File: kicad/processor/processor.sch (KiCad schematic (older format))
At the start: 24 parts

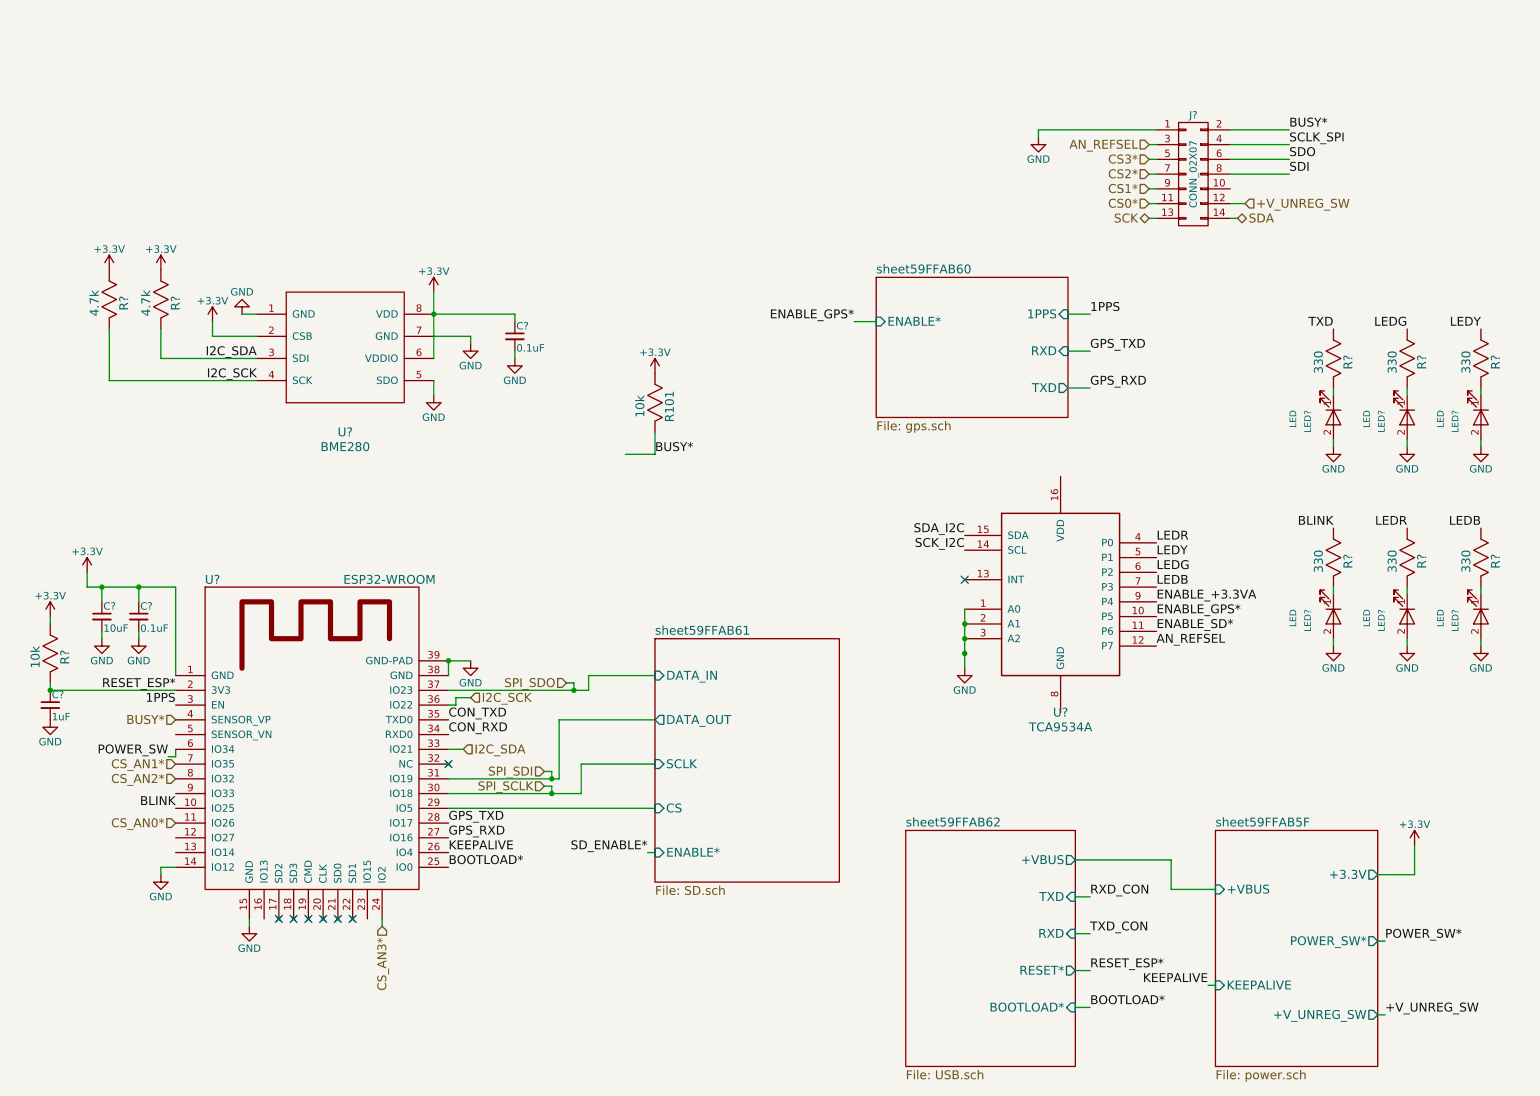
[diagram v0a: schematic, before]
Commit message: Finish split projects, fix ERC, import outline to processor board
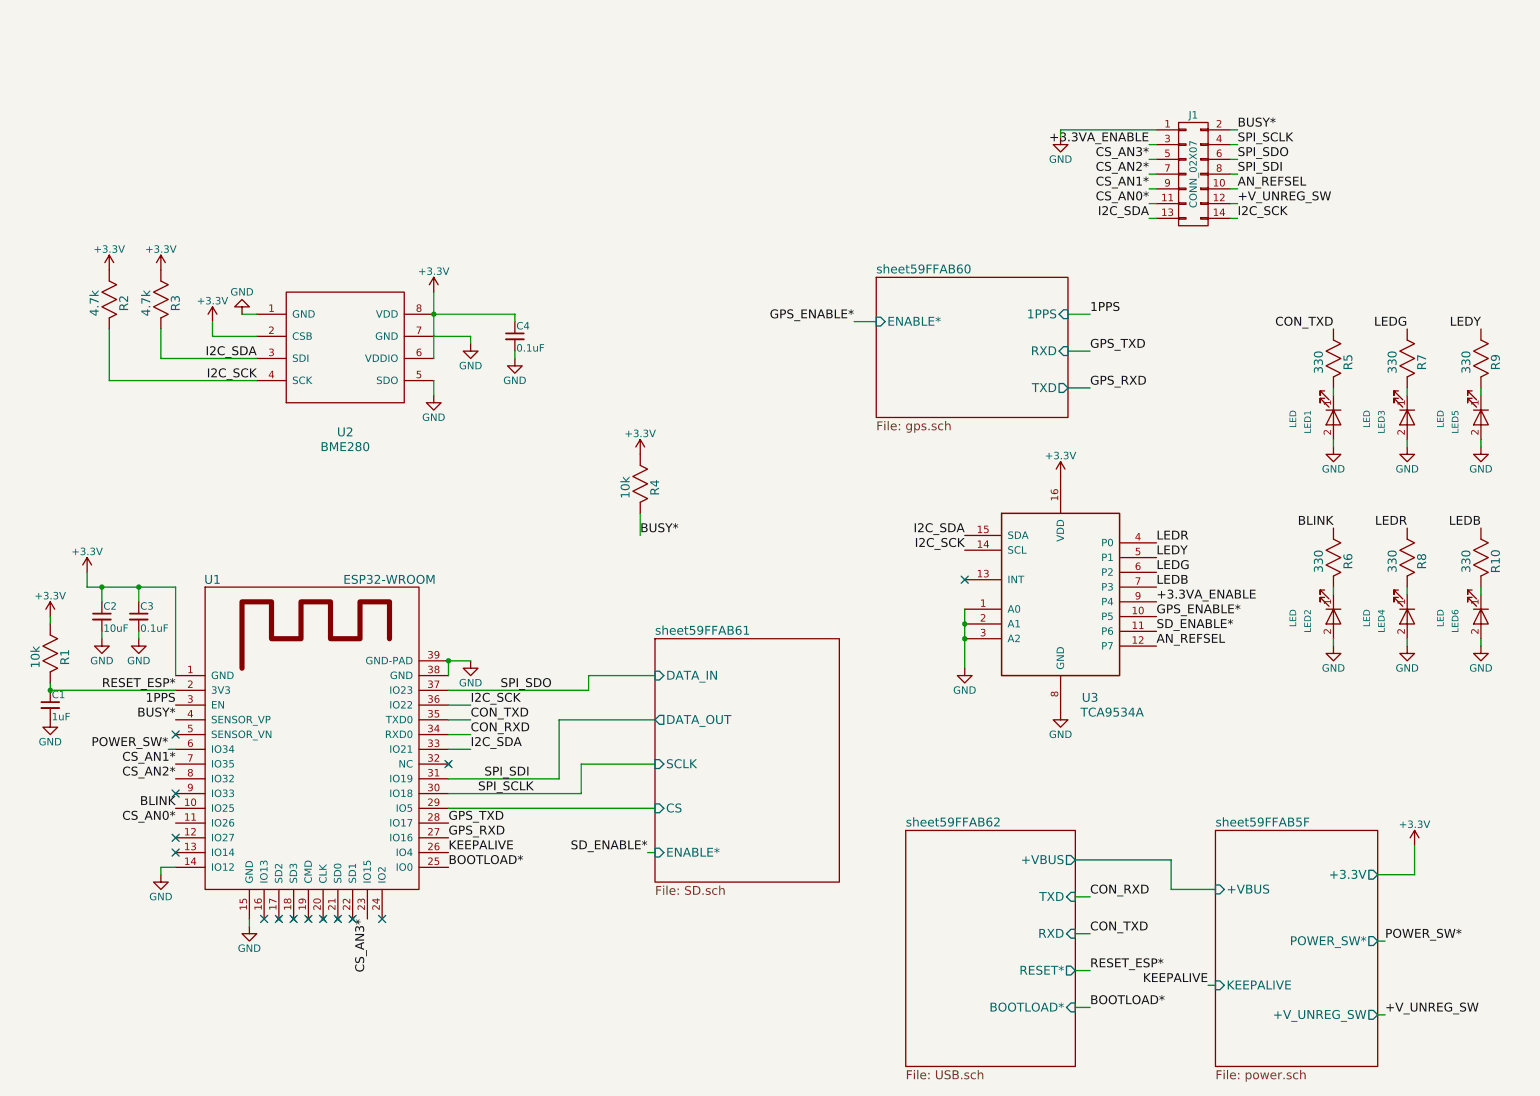
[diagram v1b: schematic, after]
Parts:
- gave numbers to parts that had none: 23
- renumbered R101 to R4
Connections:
- net CS0* is gone; now on net CS_AN0*: J1.11 (P11)
- net CS1* is gone; now on net CS_AN1*: J1.9 (P9)
- net CS2* is gone; now on net CS_AN2*: J1.7 (P7)
- net CS3* is gone; now on net CS_AN3*: J1.5 (P5)
- net ENABLE_SD* is gone; now on net SD_ENABLE*: U3.11 (P6)
- net POWER_SW is gone; now on net POWER_SW*: U1.6 (IO34)
- net SCK is gone; now on net I2C_SDA: J1.13 (P13)
- net SCK_I2C is gone; now on net I2C_SCK: U3.14 (SCL)
- net SCLK_SPI is gone; now on net SPI_SCLK: J1.4 (P4)
- net SDA is gone; now on net I2C_SCK: J1.14 (P14)
- net SDA_I2C is gone; now on net I2C_SDA: U3.15 (SDA)
- net SDI is gone; now on net SPI_SDI: J1.8 (P8)
- net SDO is gone; now on net SPI_SDO: J1.6 (P6)
- net TXD is gone; now on net CON_TXD: R5.1
- net +3V3: now also U3.16 (VDD)
- net AN_REFSEL: now also J1.10 (P10); no longer J1.3 (P3)
- net CS_AN3*: now also U1.23 (IO15); no longer U1.24 (IO2)
- net GND: now also U3.8 (GND)
- net ENABLE_+3.3VA renamed +3.3VA_ENABLE
- net +3.3VA_ENABLE: now also J1.3 (P3)
- net ENABLE_GPS* renamed GPS_ENABLE*
- no-connect marks 8 -> 14
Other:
- moved on the sheet: R4

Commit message: Logic board standalone about done, changed to 0603 resistors and 0805 caps
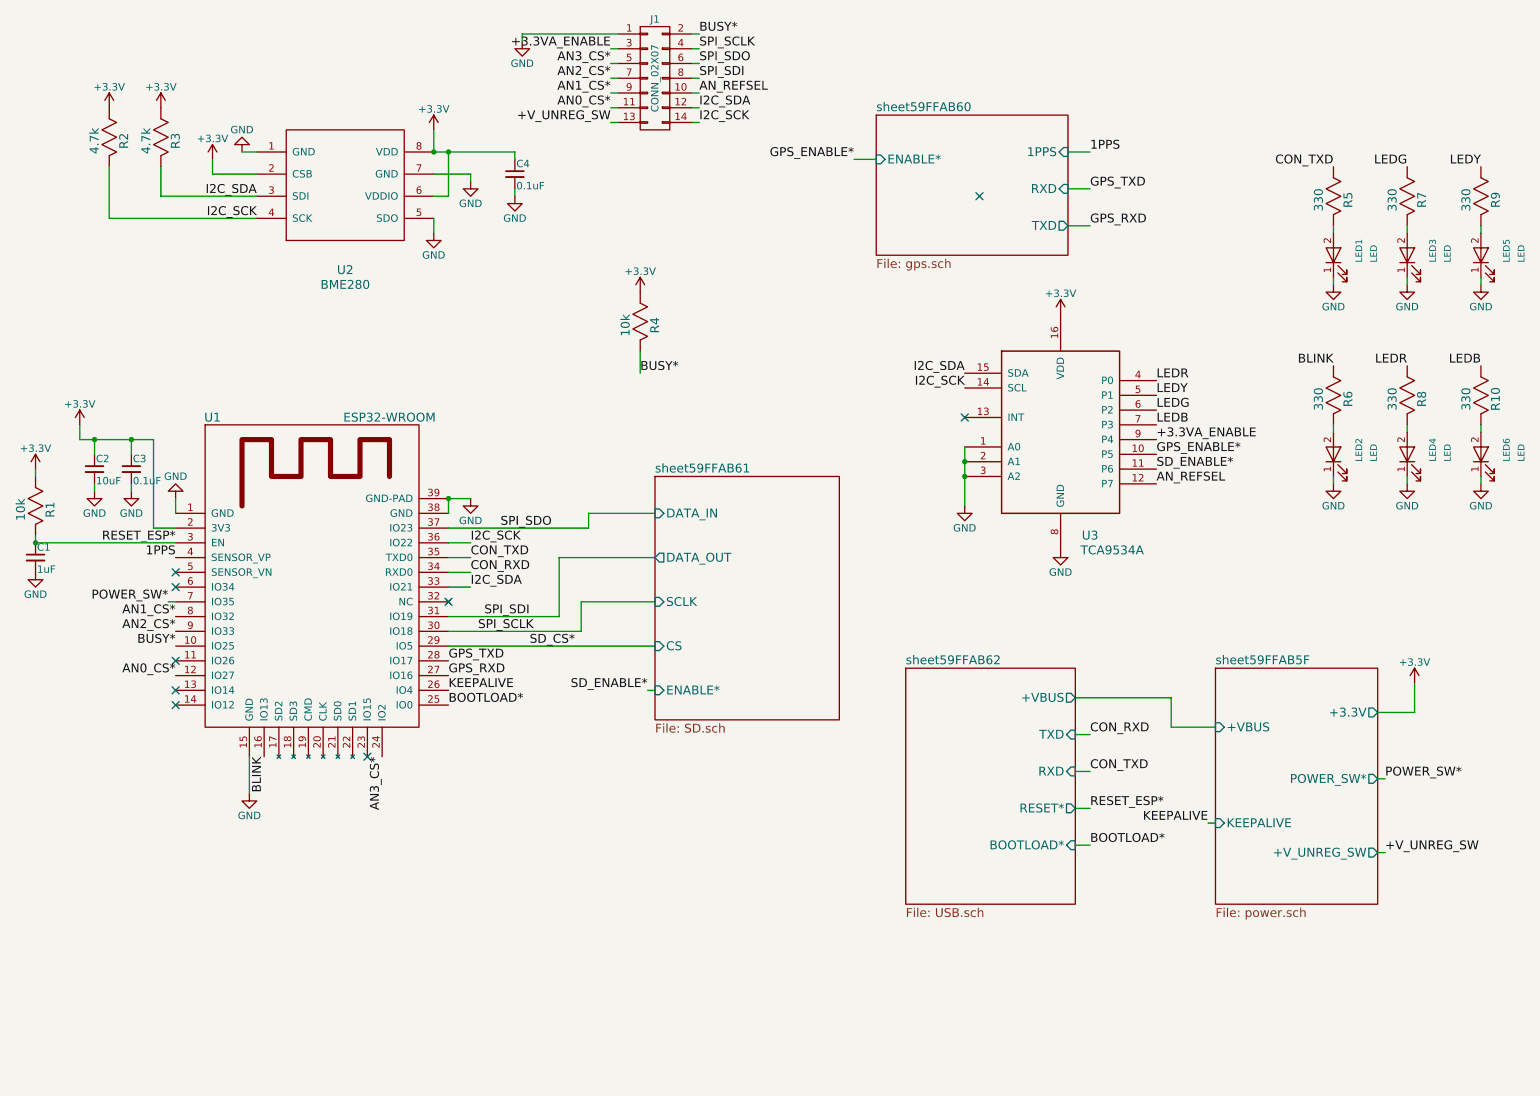
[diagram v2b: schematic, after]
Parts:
- C2: footprint paddle:SMD_1206 -> paddle:SMD_0805
- R1, R10, R2, R3, R4, R5, R6, R7, R8, R9: footprint paddle:SMD_0805 -> paddle:R_0603
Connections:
- net +3V3: now also U1.2 (3V3); no longer U1.1 (GND)
- net +V_UNREG_SW: now also J1.13 (P13); no longer J1.12 (P12)
- net 1PPS: now also U1.4 (SENSOR_VP); no longer U1.3 (EN)
- net BLINK: now also U1.16 (IO13); no longer U1.10 (IO25)
- net BUSY*: now also U1.10 (IO25); no longer U1.4 (SENSOR_VP)
- net GND: now also LED1.1 (K), LED2.1 (K), LED3.1 (K), LED4.1 (K), LED5.1 (K), LED6.1 (K), U1.1 (GND); no longer LED1.2 (A), LED2.2 (A), LED3.2 (A), LED4.2 (A), LED5.2 (A), LED6.2 (A), U1.14 (IO12)
- net I2C_SDA: now also J1.12 (P12); no longer J1.13 (P13)
- net POWER_SW*: now also U1.7 (IO35); no longer U1.6 (IO34)
- net RESET_ESP*: now also U1.3 (EN); no longer U1.2 (3V3)
- net at R7.2: now also LED3.2 (A); no longer LED3.1 (K)
- net at R9.2: now also LED5.2 (A); no longer LED5.1 (K)
- net at R8.2: now also LED4.2 (A); no longer LED4.1 (K)
- net at R10.2: now also LED6.2 (A); no longer LED6.1 (K)
- net AN0_CS*: now reaches U1.12 (IO27)
- net AN0_CS*: now also J1.11 (P11)
- net AN3_CS*: now reaches U1.24 (IO2)
- net AN3_CS*: now also J1.5 (P5)
- net AN2_CS*: now reaches U1.9 (IO33)
- net AN2_CS*: now also J1.7 (P7)
- net at R5.2: now also LED1.2 (A); no longer LED1.1 (K)
- net at R6.2: now also LED2.2 (A); no longer LED2.1 (K)
- net CS_AN0*: no longer names the net of U1.11 (IO26)
- net CS_AN0*: no longer J1.11 (P11)
- net CS_AN1* renamed AN1_CS*
- net AN1_CS*: now also U1.8 (IO32); no longer U1.7 (IO35)
- removed net CS_AN2*: J1.7 (P7), U1.8 (IO32)
- net CS_AN3*: no longer names the net of U1.23 (IO15)
- net CS_AN3*: no longer J1.5 (P5)
- net sheet59FFAB61/CS renamed SD_CS*
- no-connect marks 14 -> 9
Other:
- moved on the sheet: C1, C2, C3, C4, J1, LED1, LED2, LED3, LED4, LED5, LED6, R1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
